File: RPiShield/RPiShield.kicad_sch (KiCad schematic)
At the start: 4 parts, among them J2 BBOX, J4 Corridor1, J7 FC68148, J8 2223

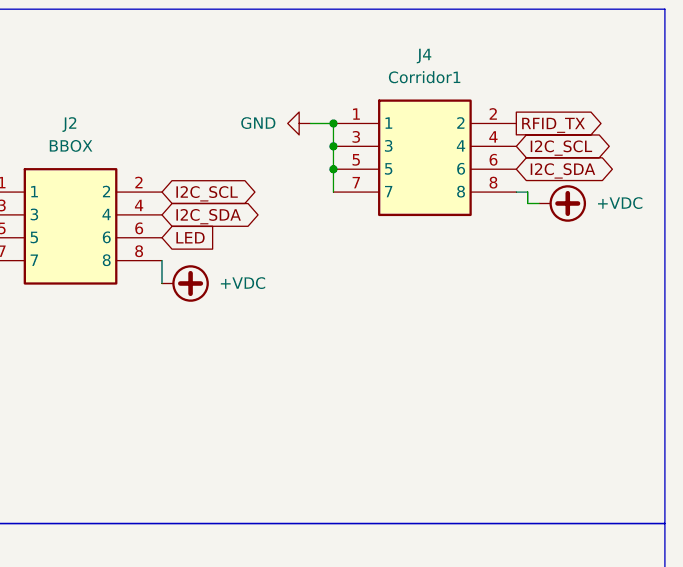
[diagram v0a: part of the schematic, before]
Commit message: Adding fuseholder to the HAT
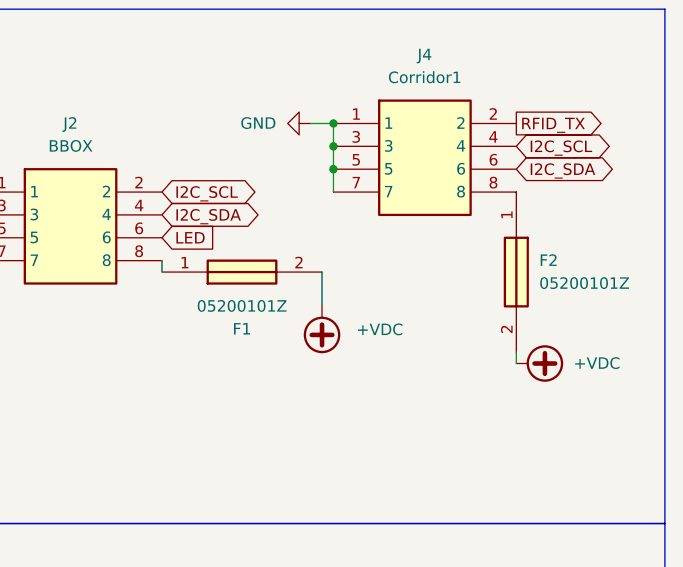
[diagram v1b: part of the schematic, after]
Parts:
- added F1, F2: 05200101Z, 05200101Z, symbol 05200101Z:05200101Z
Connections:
- net +VDC: now also F1.2, F2.2; no longer J2.8, J4.8
- new net: F1.1, J2.8
- new net: F2.1, J4.8
